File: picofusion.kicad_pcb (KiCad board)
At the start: 4 copper layers, 25.5 x 25.5 mm, 53 parts, among them J1 NORTH, J2 EAST, J3 WEST, J4 SOUTH, U1 W25Q16, U2 RP2040, U3 TLV71333PDQNT, U4 ICM42605, U5 MMC5983MA, U6 ICP20100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

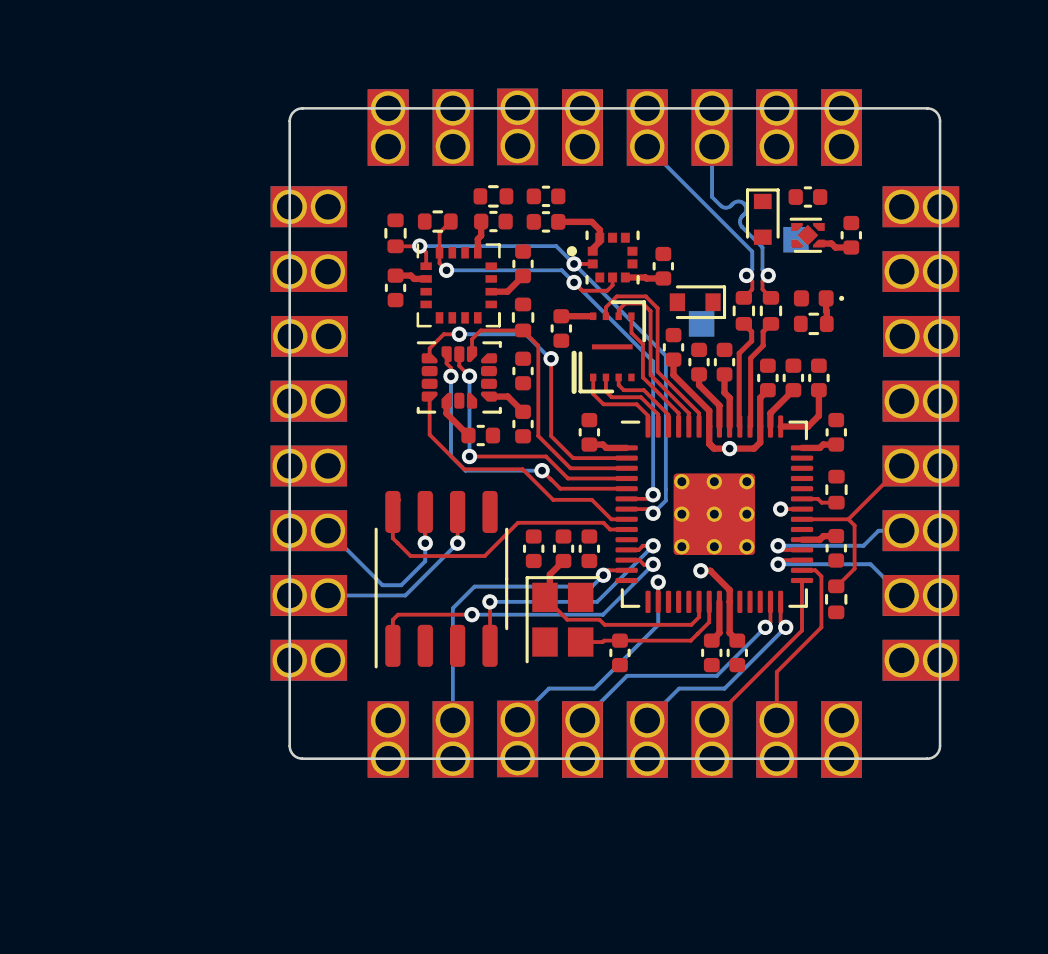
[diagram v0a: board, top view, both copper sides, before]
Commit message: Add traces to various components
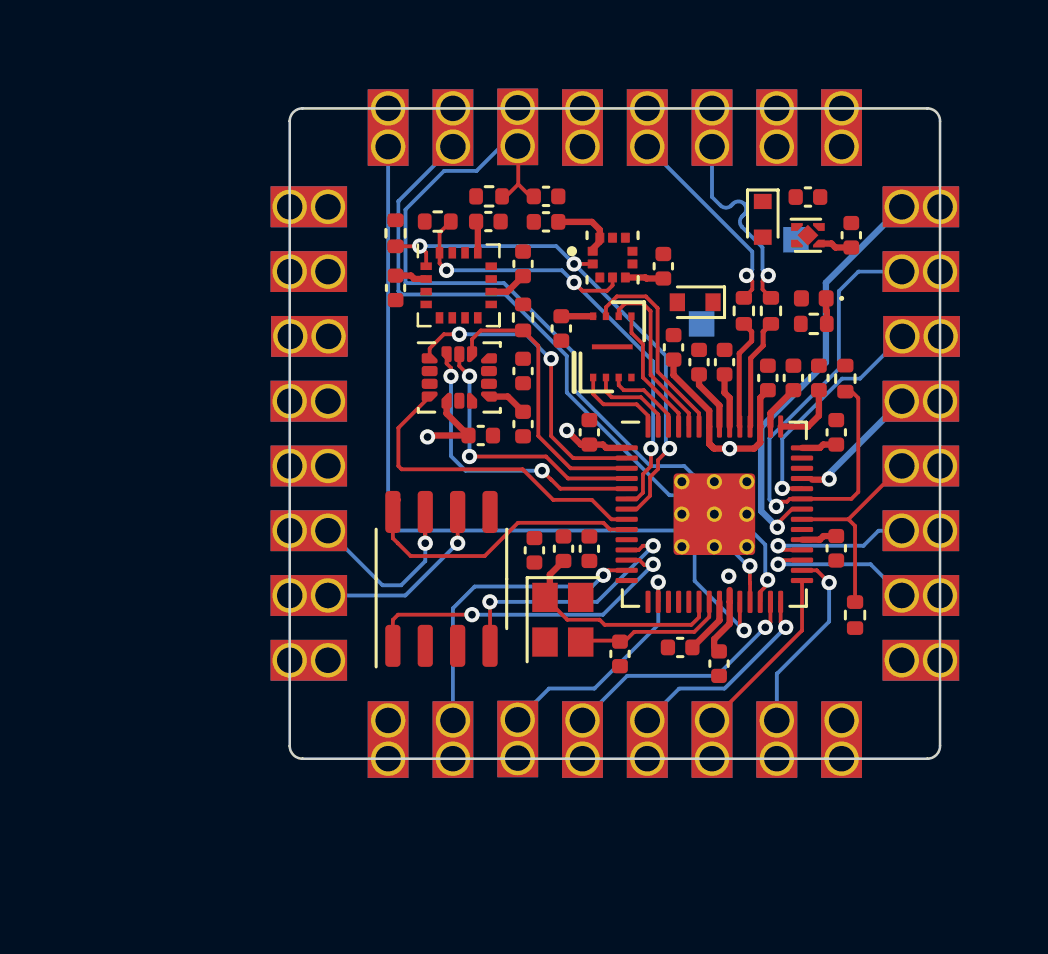
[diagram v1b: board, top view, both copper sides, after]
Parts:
- moved R4 4.37 mm to (169.0, 37.8)
- moved C9 1.26 mm to (162.6, 48.4), turned to 180 degrees
- moved R5 0.96 mm to (169.4, 47.1)
- moved C2 0.83 mm to (164.1, 49.0)
- moved C21 0.20 mm to (155.0, 31.7)
- moved R1 0.17 mm to (155.1, 30.7)
- moved C27 0.07 mm to (156.8, 44.6)
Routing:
- net /RUN: track 0.00 -> 33.4 mm, vias 0 -> 1
- net /SWCLK: track 0.00 -> 32.6 mm, vias 0 -> 1
- net /SWDIO: track 0.00 -> 27.5 mm, vias 0 -> 1
- net /SPI1_nCS_SD: track 1.41 -> 20.0 mm, vias 0 -> 1
- net /SPI1_POCI_SD: track 0.86 -> 16.5 mm
- net /SPI1_SCK_SD: track 0.00 -> 9.10 mm, vias 0 -> 1
- net /SPI1_PICO_SD: track 0.00 -> 4.91 mm, vias 0 -> 1
- net +3V3: track 26.2 -> 29.5 mm, vias 0 -> 2
- net /DRDY_ICM42605: track 10.6 -> 13.0 mm
- net +1V1: track 17.5 -> 16.2 mm
- net /UART0_RTS_TELEM: track 7.24 -> 7.52 mm, vias 0 -> 1

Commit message: routing cleanup, merge minor schematic fixes
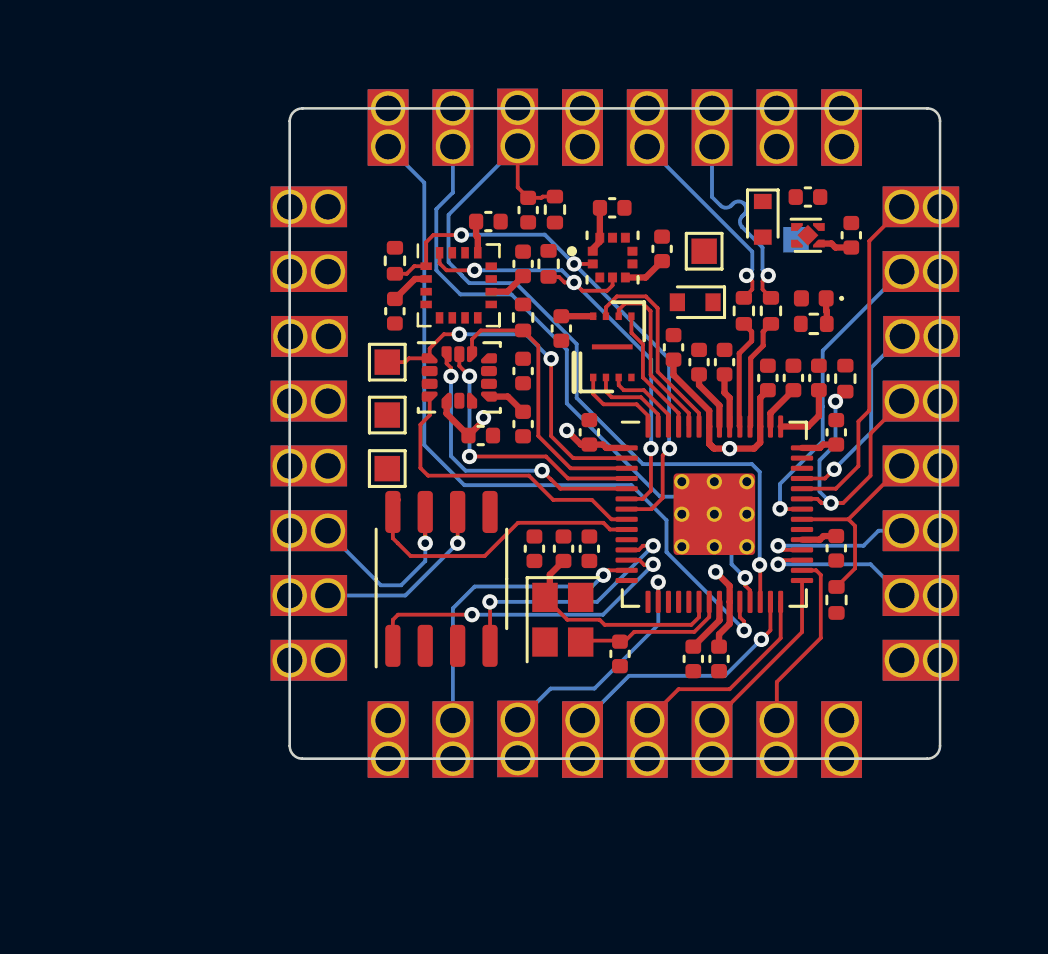
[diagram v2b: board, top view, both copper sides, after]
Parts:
- added TP2: TestPoint, TestPoint:TestPoint_Pad_1.0x1.0mm, F.Cu at (151.1, 39.3)
- added TP3: TestPoint, TestPoint:TestPoint_Pad_1.0x1.0mm, F.Cu at (151.1, 41.4)
- added TP4: TestPoint, TestPoint:TestPoint_Pad_1.0x1.0mm, F.Cu at (151.1, 37.2)
- D2: value RED -> GREEN
- R8, R9: value 2.7K -> 1.5K
- TP1: moved to F.Cu
- moved R9 4.65 mm to (157.4, 33.3), turned to -90 degrees
- moved TP1 2.85 mm to (163.5, 32.9), turned to 0 degrees
- moved C23 2.65 mm to (159.9, 31.1), turned to 0 degrees
- moved R1 2.63 mm to (157.7, 31.2), turned to 90 degrees
- moved R8 1.08 mm to (151.4, 33.2)
- moved R5 0.94 mm to (168.7, 46.5)
- moved C12 0.92 mm to (151.4, 35.2)
- moved C11 0.88 mm to (156.6, 31.2), turned to -90 degrees
- moved C9 0.68 mm to (163.1, 48.8), turned to -90 degrees
- moved C22 0.68 mm to (161.8, 32.8)
- moved C2 0.18 mm to (164.1, 48.8)
- moved C27 0.06 mm to (156.8, 44.5)
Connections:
- C14 pad 1: +5V -> Net-(C14-Pad1)
- D1 pad 1: GND -> +5V
- D1 pad 2: +5V -> GND
- D3 pad 1: GND -> Net-(C14-Pad1)
- J2 pad 1: /SPI1_POCI_SD -> /SPI1_SCK_SD
- J2 pad 2: /SPI1_nCS_SD -> /SPI1_POCI_SD
- J2 pad 3: /SPI1_SCK_SD -> /SPI1_PICO_SD
- J2 pad 4: /SPI1_PICO_SD -> /SPI1_nCS_SD
- U3 pad 1: +5V -> Net-(C14-Pad1)
- U3 pad 3: +5V -> Net-(C14-Pad1)
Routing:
- net /SPI1_nCS_SD: track 20.0 -> 12.3 mm, vias 1 -> 2
- net +1V1: track 16.2 -> 11.8 mm
- net /SPI1_SCK_SD: track 9.10 -> 13.4 mm, vias 1 -> 0
- net /SPI1_POCI_SD: track 16.5 -> 12.1 mm
- net /SPI1_PICO_SD: track 4.91 -> 7.73 mm
- net /SWCLK: track 32.6 -> 29.8 mm
- net /RUN: track 33.4 -> 30.9 mm
- net /SPI0_POCI: track 12.1 -> 13.9 mm
- net /SWDIO: track 27.5 -> 25.9 mm
- net Net-(C14-Pad1): track 0.00 -> 1.33 mm
- net +5V: track 1.33 -> 0.00 mm
- net /DRDY_ICM42605: track 13.0 -> 11.9 mm
- net +3V3: track 29.5 -> 28.4 mm
- net /I2C0_SCL: track 21.0 -> 21.8 mm
- net /UART0_RTS_TELEM: track 7.52 -> 7.23 mm, vias 1 -> 0
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
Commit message: Replace current transceiver with TJA1051TK/3118 and add work on GND/power routing
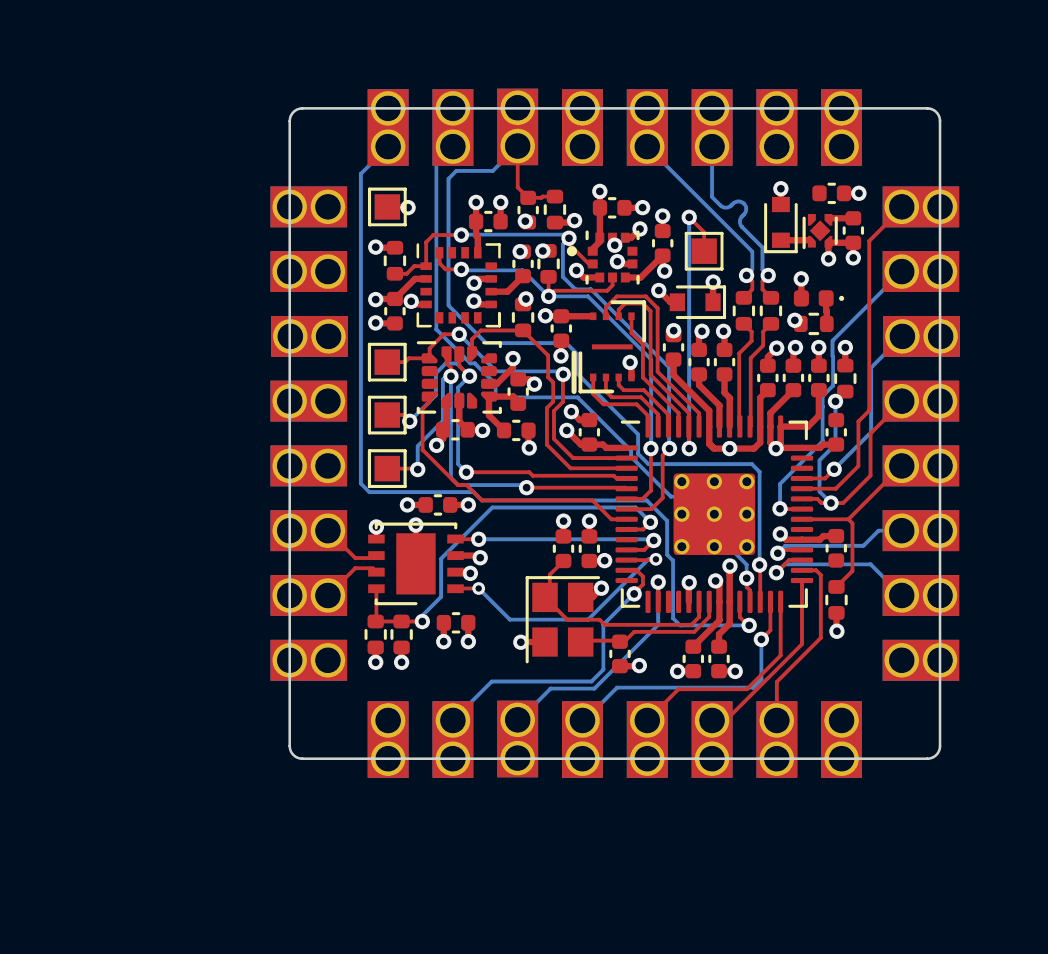
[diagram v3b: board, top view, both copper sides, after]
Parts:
- added C28: 0.1 µF, Capacitor_SMD:C_0402_1005Metric, F.Cu at (153.1, 42.8)
- added R10: 100K, Resistor_SMD:R_0402_1005Metric, F.Cu at (151.6, 47.9)
- added R11: 100K, Resistor_SMD:R_0402_1005Metric, F.Cu at (150.6, 47.9)
- 3V3: moved to F.Cu
- U7: value MCP2544FD -> TJA1051TK-3; footprint Package_SO:SOP-8_3.9x4.9mm_P1.27mm -> Package_DFN_QFN:DFN-8-1EP_3x3mm_P0.65mm_EP1.55x2.4mm
- moved 3V3 16.1 mm to (151.1, 31.1), turned to 0 degrees
- moved C27 4.23 mm to (153.8, 47.4), turned to 180 degrees
- moved U7 1.16 mm to (152.2, 45.1), turned to 180 degrees
- moved C19 1.02 mm to (153.7, 39.9)
- moved C16 0.94 mm to (168.5, 30.6)
- moved C18 0.83 mm to (156.2, 38.4)
- moved D3 0.72 mm to (166.5, 31.7), turned to 90 degrees
- moved U3 0.51 mm to (168.1, 32.0), turned to 90 degrees
- moved C17 0.37 mm to (156.1, 39.9), turned to 180 degrees
- moved C22 0.22 mm to (161.9, 32.5)
- moved C14 0.20 mm to (169.3, 32.0), turned to -90 degrees
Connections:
- net /CAN_STBY renamed /CAN_SILENT
- C27 pad 1: +5V -> +3V3
- J3 pad 6: /CAN_P -> /CAN_N
- J3 pad 7: /CAN_N -> /CAN_P
- U7 pad 5: unconnected-(U7-Pad5) -> +3V3
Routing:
- net GND: track 0.00 -> 32.2 mm, vias 0 -> 45
- net +3V3: track 28.4 -> 44.4 mm, vias 2 -> 21
- net /QSPI_SCLK: track 6.87 -> 18.4 mm, vias 0 -> 2
- net /CAN_P: track 8.26 -> 2.22 mm, vias 1 -> 0
- net /SPI0_PICO: track 11.5 -> 17.5 mm, vias 2 -> 3
- net /SPI0_SCK: track 10.7 -> 16.7 mm, vias 2 -> 3
- net /CAN_SILENT: track 11.1 -> 16.2 mm, vias 0 -> 2
- net /CAN_N: track 7.17 -> 2.22 mm, vias 1 -> 0
- net +1V1: track 11.8 -> 16.6 mm
- net /SWCLK: track 29.8 -> 34.4 mm
- net +5V: track 0.00 -> 3.13 mm, vias 0 -> 4
- net /PIO0_CAN_TX: track 13.3 -> 10.5 mm
- net /I2C0_SCL: track 21.8 -> 23.6 mm
- net /RUN: track 30.9 -> 32.4 mm
- net /PIO0_CAN_RX: track 10.1 -> 9.01 mm
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
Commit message: layout: cleanup, planes, some drc
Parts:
- moved TP1 22.3 mm to (141.7, 28.6)
- moved TP4 12.7 mm to (138.7, 34.8)
- moved TP2 8.74 mm to (142.3, 38.7)
- moved TP3 7.39 mm to (143.7, 41.9)
- moved 3V3 7.32 mm to (143.9, 29.7)
- moved R9 5.88 mm to (151.8, 31.7), turned to 0 degrees
- moved C27 5.30 mm to (151.7, 42.5), turned to 0 degrees
- moved C5 4.62 mm to (155.8, 48.6), turned to -90 degrees
- moved C28 3.55 mm to (156.5, 43.8), turned to 0 degrees
- moved R5 2.92 mm to (168.7, 43.6)
- moved R11 1.57 mm to (151.9, 48.8), turned to 180 degrees
- moved C15 1.50 mm to (168.7, 46.0)
- moved C2 1.15 mm to (165.1, 48.3), turned to 0 degrees
- moved C6 0.93 mm to (158.4, 43.8), turned to 180 degrees
- moved C21 0.89 mm to (154.1, 31.7), turned to 180 degrees
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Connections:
- U2 pad 13: /IMU_HEATER -> /CAN_SILENT
- U2 pad 14: unconnected-(U2-Pad14) -> /IMU_HEATER
- U2 pad 9: /CAN_SILENT -> unconnected-(U2-Pad9)
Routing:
- net /QSPI_SCLK: track 18.4 -> 6.87 mm, vias 2 -> 0
- net /SPI0_SCK: track 16.7 -> 11.1 mm, vias 3 -> 2
- net /SPI0_PICO: track 17.5 -> 12.0 mm, vias 3 -> 2
- net GND: track 32.2 -> 37.3 mm, vias 45 -> 41
- net /I2C0_SDA: track 20.3 -> 25.1 mm
- net /PIO0_CAN_TX: track 10.5 -> 6.48 mm, vias 2 -> 0
- net /RUN: track 32.4 -> 28.6 mm
- net /CAN_SILENT: track 16.2 -> 12.6 mm, vias 2 -> 0
- net /SD_nCD: track 7.76 -> 4.78 mm
- net /PIO0_CAN_RX: track 9.01 -> 6.19 mm, vias 2 -> 0
- net /I2C0_SCL: track 23.6 -> 26.4 mm
- net /SWCLK: track 34.4 -> 31.8 mm
- net /UART1_TX_GNSS: track 6.77 -> 4.49 mm, vias 1 -> 0
- net /SPI0_POCI: track 14.1 -> 11.9 mm
- net /UART1_RX_GNSS: track 6.23 -> 4.24 mm, vias 1 -> 0
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- added copper zone on In2.Cu, net +3V3
- added copper zone on In1.Cu, net GND

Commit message: Finish R01A
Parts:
- removed TP1: QSPI_SCK, TestPoint:TestPoint_Pad_1.0x1.0mm
- removed TP2, TP3, TP4: TestPoint, TestPoint:TestPoint_Pad_1.0x1.0mm
- added G***: LOGO, Logos:amadoruavs_logo_smol, B.Cu at (153.8, 36.9)
- added R12: 0, Resistor_SMD:R_0402_1005Metric, F.Cu at (153.7, 47.6)
- added R13: 0, Resistor_SMD:R_0402_1005Metric, F.Cu at (153.7, 42.7)
- added R14: 0, Resistor_SMD:R_0402_1005Metric, F.Cu at (151.3, 31.3)
- added R15: 0, Resistor_SMD:R_0402_1005Metric, F.Cu at (151.3, 39.5)
- added R16: 0, Resistor_SMD:R_0402_1005Metric, F.Cu at (151.3, 37.4)
- added R17: 0, Resistor_SMD:R_0402_1005Metric, F.Cu at (151.8, 41.1)
- added REF**: OSHW-Logo2_7.3x6mm_SilkScreen, Symbol:OSHW-Logo2_7.3x6mm_SilkScreen, B.Cu at (153.9, 44.2)
- C27, C28: value 0.1 µF -> 0.1uF
- U3: value TLV71333PDQNT -> TLV71333PDQN
- moved 3V3 20.2 mm to (163.5, 34.5)
- moved D1 2.99 mm to (164.1, 32.0), turned to -90 degrees
- moved C16 2.80 mm to (167.4, 33.1)
- moved R9 1.30 mm to (153.1, 31.6)
- moved R10 1.19 mm to (150.9, 48.3), turned to -90 degrees
- moved D3 0.95 mm to (165.6, 32.0)
- moved U3 0.85 mm to (167.4, 31.5)
- moved C21 0.81 mm to (154.9, 31.6), turned to 0 degrees
- moved C14 0.70 mm to (168.9, 31.5)
- moved R11 0.50 mm to (151.9, 48.4), turned to 90 degrees
- moved C27 0.15 mm to (151.7, 42.7)
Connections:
- J3 pad 1: unconnected-(J3-Pad1) -> /SDA/SDI
- J3 pad 2: unconnected-(J3-Pad2) -> /SCL/SCK
- J3 pad 3: unconnected-(J3-Pad3) -> /SPI0_POCI
- J3 pad 4: GND -> /NEOPIXEL
- U2 pad 17: /NEOPIXEL -> unconnected-(U2-Pad17)
- U2 pad 9: unconnected-(U2-Pad9) -> /NEOPIXEL
- U3 pad 1: Net-(C14-Pad1) -> +3V3
- U3 pad 4: unconnected-(U3-Pad4) -> Net-(C14-Pad1)
- U3 pad 5: +3V3 -> GND
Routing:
- net +5V: track 2.52 -> 34.6 mm
- net /NEOPIXEL: track 0.00 -> 18.7 mm, vias 0 -> 1
- net /SDA/SDI: track 0.00 -> 11.0 mm, vias 0 -> 2
- net /SCL/SCK: track 0.00 -> 10.1 mm, vias 0 -> 1
- net /I2C0_SCL: track 26.4 -> 32.8 mm
- net /SPI0_POCI: track 11.9 -> 17.2 mm
- net /CAN_P: track 3.08 -> 6.45 mm
- net /CAN_N: track 3.11 -> 6.30 mm
- net GND: track 37.3 -> 34.3 mm, vias 41 -> 40
- net /SPI0_SCK: track 11.1 -> 13.9 mm, vias 2 -> 3
- net /SPI0_PICO: track 12.0 -> 14.7 mm, vias 2 -> 3
- net Net-(C14-Pad1): track 2.23 -> 0.00 mm
- net +3V3: track 43.7 -> 45.7 mm, vias 23 -> 26
- net /PIO0_CAN_TX: track 6.48 -> 8.10 mm
- net /PIO0_CAN_RX: track 6.19 -> 7.73 mm
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- added copper zone on B.Cu, net GND
- added copper zone on F.Cu, net GND
- added copper zone on F.Cu, net Net-(C14-Pad1)
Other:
- board text added: "Designed by: Kalyan Sriram Kush Nayak Vincent Wang"
- board text added: "JLCJLCJLCJLC"
- board text added: "MOD-PICOFUSION-R01A"
- board text added: "PicoFusion AHRS"

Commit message: Finish R01B
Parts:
- added C29: 0.1uF, Capacitor_SMD:C_0402_1005Metric, F.Cu at (152.8, 40.1)
- U4: value ICM42605 -> ICM-20602; footprint Package_LGA:LGA-14_3x2.5mm_P0.5mm_LayoutBorder3x4y -> Package_LGA:LGA-16_3x3mm_P0.5mm_LayoutBorder3x5y
- moved C19 3.39 mm to (156.2, 37.8), turned to 90 degrees
- moved C18 1.32 mm to (156.2, 39.7)
- moved C17 1.22 mm to (154.7, 40.1)
- moved REF** 0.70 mm to (153.9, 43.5)
- moved R17 0.20 mm to (151.8, 41.3)
- turned U4 to 180 degrees
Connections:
- U2 pad 8: /DRDY_ICM42605 -> /DRDY_ICM20602
- U4 pad 1: /SPI0_POCI -> +3V3
- U4 pad 10: unconnected-(U4-Pad10) -> GND
- U4 pad 11: unconnected-(U4-Pad11) -> GND
- U4 pad 12: /SPI0_nCS -> GND
- U4 pad 13: /SPI0_SCK -> GND
- U4 pad 14: /SPI0_PICO -> Net-(C29-Pad1)
- U4 pad 2: unconnected-(U4-Pad2) -> /SPI0_SCK
- U4 pad 3: unconnected-(U4-Pad3) -> /SPI0_PICO
- U4 pad 4: /DRDY_ICM42605 -> /SPI0_POCI
- U4 pad 5: +3V3 -> /SPI0_nCS
- U4 pad 6: GND -> /DRDY_ICM20602
- U4 pad 8: +3V3 -> GND
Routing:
- net /DRDY_ICM20602: track 0.00 -> 12.0 mm, vias 0 -> 2
- net /DRDY_ICM42605: track 11.8 -> 0.00 mm
- net GND: track 34.3 -> 38.3 mm, vias 40 -> 42
- net Net-(C29-Pad1): track 0.00 -> 1.44 mm
- net /SPI0_nCS: track 11.6 -> 10.7 mm
- net /SWDIO: track 25.7 -> 24.9 mm
- net +3V3: track 45.7 -> 45.0 mm
- net /SWCLK: track 33.0 -> 33.5 mm
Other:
- board text added: "MOD-PICOFUSION-R01B"
- board text removed: "MOD-PICOFUSION-R01A"

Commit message: more work
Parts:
- removed 3V3: TestPoint, TestPoint:TestPoint_Pad_1.0x1.0mm
- removed REF**: OSHW-Logo2_7.3x6mm_SilkScreen, Symbol:OSHW-Logo2_7.3x6mm_SilkScreen
- added R18: 0, Resistor_SMD:R_0402_1005Metric, F.Cu at (162.5, 56.7)
- added R19: 0, Resistor_SMD:R_0402_1005Metric, F.Cu at (161.9, 31.1)
- added R20: 1K, Resistor_SMD:R_0402_1005Metric, F.Cu at (157.9, 31.1)
- added R21: 10K, Resistor_SMD:R_0402_1005Metric, F.Cu at (158.0, 40.0)
- added R22: 0, Resistor_SMD:R_0402_1005Metric, F.Cu at (140.7, 42.5)
- added R23: 10K, Resistor_SMD:R_0402_1005Metric, F.Cu at (165.7, 58.0)
- moved D1 2.88 mm to (163.2, 34.8), turned to 0 degrees
- moved R1 1.43 mm to (157.4, 32.6)
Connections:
- net /QSPI_SS renamed /QSPI_nCS
- J1 pad 4: GND -> /BOOTSEL
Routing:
- net /QSPI_nCS: track 3.58 -> 16.4 mm, vias 0 -> 2
- net /BOOTSEL: track 0.00 -> 6.35 mm
- net /SPI0_POCI: track 17.1 -> 14.5 mm, vias 2 -> 1
- net /I2C0_SDA: track 25.1 -> 23.2 mm
- net /RUN: track 28.6 -> 29.5 mm
- net +3V3: track 45.0 -> 44.2 mm, vias 26 -> 25

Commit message: finish R02B
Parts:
- added R24: 0, Resistor_SMD:R_0402_1005Metric, F.Cu at (168.7, 48.0)
- moved R23 21.6 mm to (157.9, 37.9), turned to 90 degrees
- moved R22 13.0 mm to (153.7, 41.6), turned to 180 degrees
- moved R18 9.51 mm to (167.2, 48.4), turned to -90 degrees
- moved R17 0.36 mm to (151.7, 41.6)
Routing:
- net /SPI0_nCS: track 10.8 -> 29.8 mm, vias 0 -> 2
- net /SD_nCD: track 4.78 -> 10.2 mm, vias 0 -> 2
- net /RUN: track 29.5 -> 32.9 mm
- net /SPI0_POCI: track 14.5 -> 17.0 mm, vias 1 -> 2
- net /NEOPIXEL: track 18.7 -> 20.7 mm, vias 1 -> 2
- net GND: track 38.4 -> 40.4 mm, vias 42 -> 43
- net /QSPI_nCS: track 16.4 -> 17.9 mm
- net /DRDY_ICM20602: track 12.0 -> 13.3 mm
- net +3V3: track 44.2 -> 43.1 mm, vias 25 -> 26
- net /SPI0_PICO: track 15.1 -> 15.9 mm, vias 3 -> 2
- net /UART0_CTS_TELEM: track 8.33 -> 9.00 mm
- net /SDA/SDI: track 11.0 -> 10.4 mm
- net /SWDIO: track 24.9 -> 24.3 mm
- net /SWCLK: track 33.5 -> 34.1 mm
